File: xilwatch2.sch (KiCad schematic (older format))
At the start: 1 part

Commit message: More work, mostly copied from rev1
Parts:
- added BT?: Battery_Cell, symbol Device:Battery_Cell
- added C? (x5): 0.1uF, symbol Device:C_Small
- added D?: LED_TopLeft, symbol Device_Extra:LED_RGBA
- added D?: LED_TopRight, symbol Device_Extra:LED_RGBA
- added D?: LED_BottomLeft, symbol Device_Extra:LED_RGBA
- added D?: LED_BottomRight, symbol Device_Extra:LED_RGBA
- added J?: Conn_SWD, symbol Connector_Generic:Conn_01x04
- added M?: Vibrator, symbol Motor:Motor_DC
- added Q?: BSS138, Package_TO_SOT_SMD:SOT-23, symbol Transistor_FET:BSS138
- added R? (x2): 10K, symbol Device:R_Small
- added R? (x12): 360R, symbol Device:R_Small
- added SW?: Btn_Up, symbol Switch:SW_Push
- added SW?: Btn_Select, symbol Switch:SW_Push
- added SW?: Btn_Down, symbol Switch:SW_Push
- added SW?: Btn_Back, symbol Switch:SW_Push
- added U?: MPU-6500, symbol Sensor_Motion_Extra:MPU-6500
- added U?: LPH7366, symbol Display_Graphic_Extra:LPH7366
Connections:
- net labels added: +BATT, BTN_BACK, BTN_DOWN, BTN_SELECT, BTN_UP, LCD_CS, LCD_DC, LCD_DIN, LCD_RESET, LCD_SCK, LED1_B, LED1_G, LED1_R, LED2_B, LED2_G, LED2_R, LED3_B, LED3_G, LED3_R, LED4_B, LED4_G, LED4_R, MPU_INT, MPU_SCL, MPU_SDA, SWDCLK, SWDIO, VDD, VIBRATOR
- wire segments 50 -> 147
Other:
- note added: "TODO:\n- USB connector\n- power stuff\n- USB connector\n- debug connector\n- LEDs\n- connectivity?\n- speaker?"

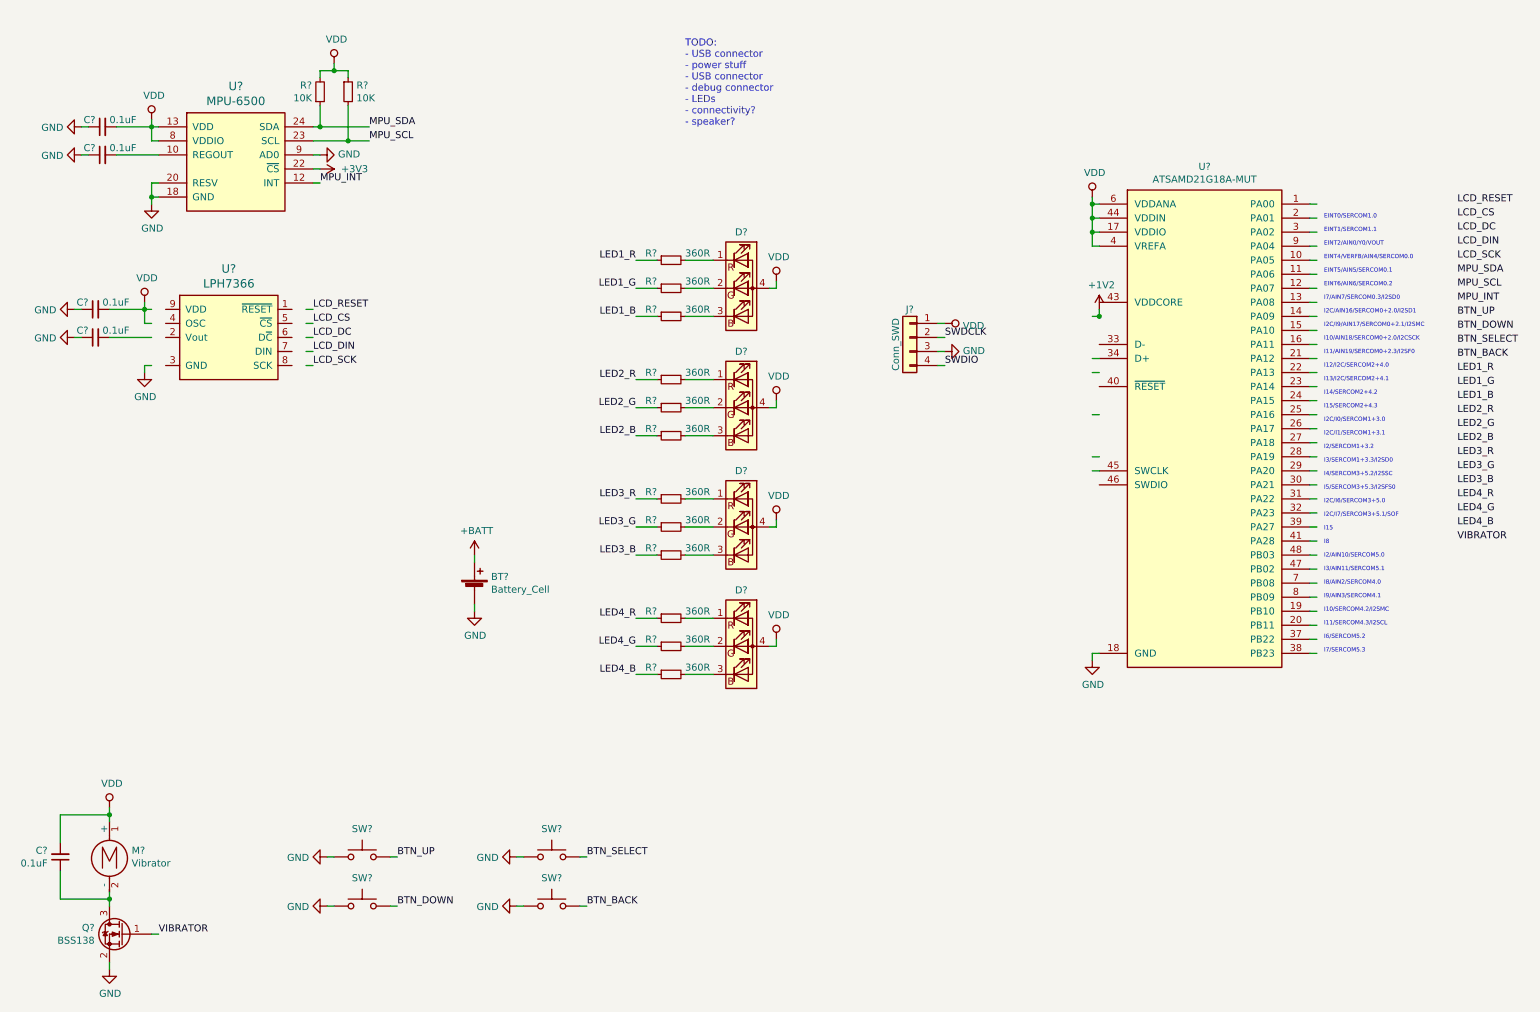
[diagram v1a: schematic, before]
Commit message: Finish power, usb, replace accel, add flash and assign footprints
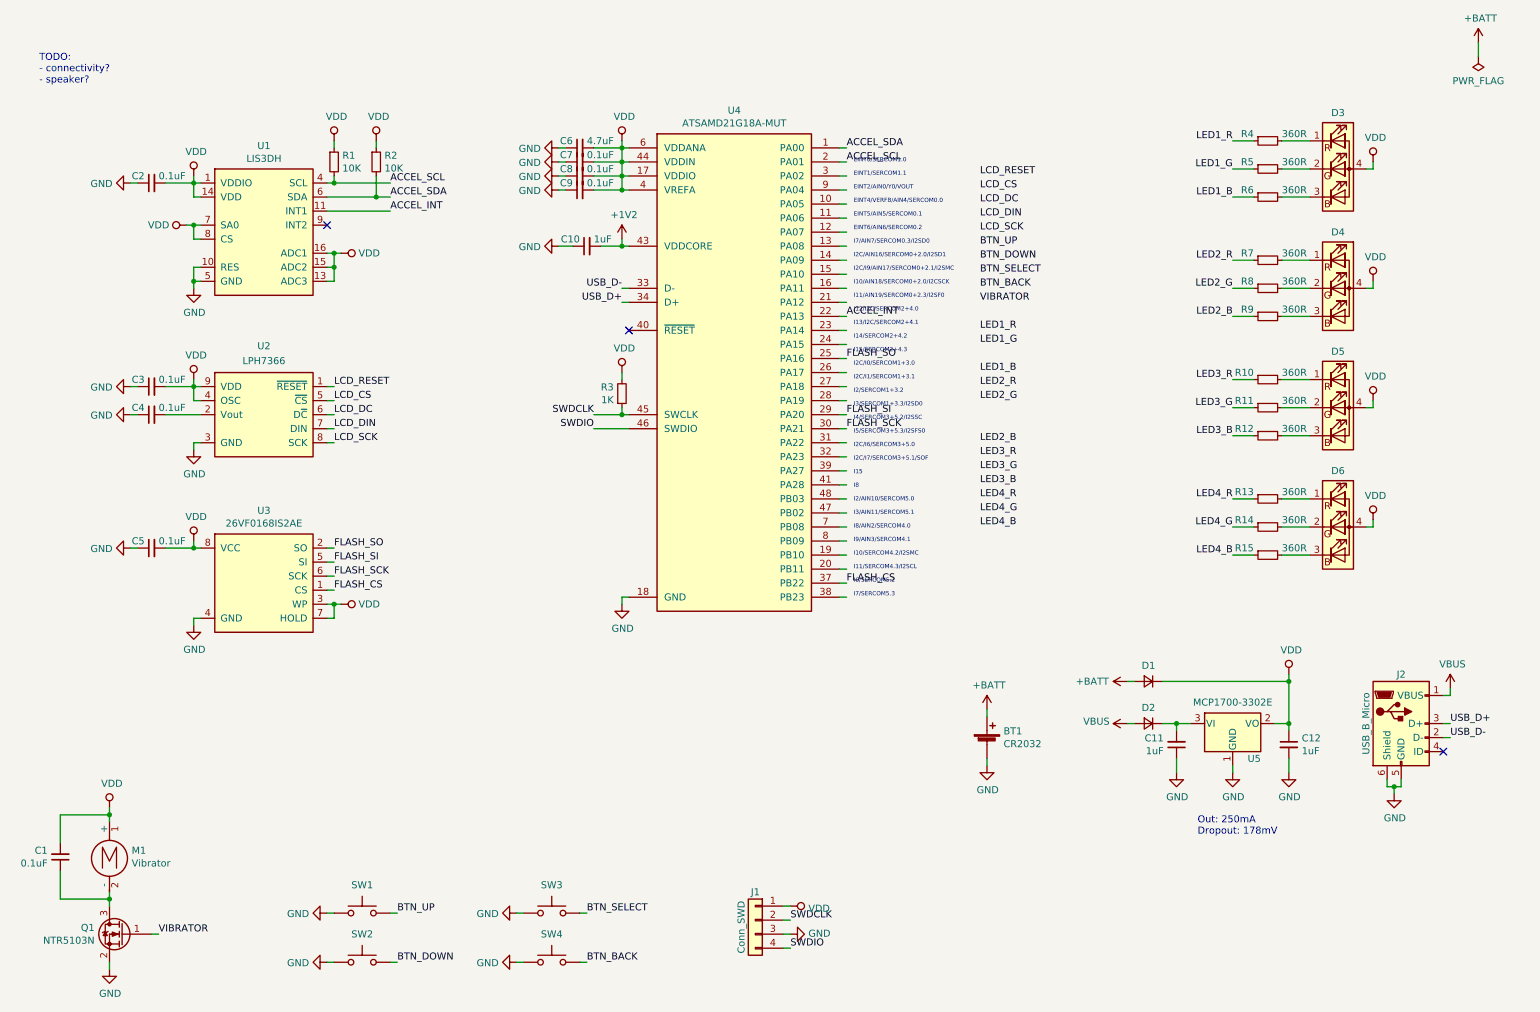
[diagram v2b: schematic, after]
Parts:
- removed C? (x2): 0.1uF, symbol Device:C_Small
- removed R? (x2): 10K, symbol Device:R_Small
- removed U?: MPU-6500, symbol Sensor_Motion_Extra:MPU-6500
- added C10, C11, C12: 1uF, Capacitor_SMD:C_0603_1608Metric, symbol Device:C_Small
- added C2, C5, C7, C8, C9: 0.1uF, Capacitor_SMD:C_0603_1608Metric, symbol Device:C_Small
- added C6: 4.7uF, Capacitor_SMD:C_0603_1608Metric, symbol Device:C_Small
- added D1, D2: S1JHE, Diode_SMD:D_SOD-323F, symbol Device:D_Small
- added J2: USB_B_Micro, Connector_USB:USB_Micro-B_Molex-105017-0001, symbol Connector:USB_B_Micro
- added R1, R2: 10K, Resistor_SMD:R_0603_1608Metric, symbol Device:R_Small
- added R3: 1K, Resistor_SMD:R_0603_1608Metric, symbol Device:R_Small
- added U1: LIS3DH, Package_LGA:LGA-16_3x3mm_P0.5mm_LayoutBorder3x5y, symbol Sensor_Motion_Extra:LIS3DH
- added U3: 26VF0168IS2AE, Package_SO:SOIJ-8_5.3x5.3mm_P1.27mm, symbol Memory_Flash_Extra:26VF0168IS2AE
- added U5: MCP1700-3302E, Package_TO_SOT_SMD:SOT-23, symbol Regulator_Linear:MCP1700-3302E_SOT23
- BT1: renamed from BT?; value Battery_Cell -> CR2032; footprint (none) -> Battery_Extra:BAT-HLD-001
- C1, C3, C4: renamed from C?; footprint (none) -> Capacitor_SMD:C_0603_1608Metric
- D3, D4, D5, D6: renamed from D?; footprint (none) -> LED_SMD_Extra:LED_RGBA_0606
- J1: renamed from J?; footprint (none) -> Connector_JST:JST_SH_SM04B-SRSS-TB_1x04-1MP_P1.00mm_Horizontal
- M1: renamed from M?; footprint (none) -> Buzzer_Beeper_Extra:C1026B
- Q1: renamed from Q?; value BSS138 -> NTR5103N
- R10, R11, R12, R13, R14, R15, R4, R5, R6, R7, R8, R9: renamed from R?; footprint (none) -> Resistor_SMD:R_0603_1608Metric
- SW1, SW2, SW3, SW4: renamed from SW?; footprint (none) -> Button_Switch_SMD_Extra:KLS7-TS2402
- U2: renamed from U?; footprint (none) -> Display_Extra:Nokia_5110-3310_LCD
- gave numbers to parts that had none: 1
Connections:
- net labels added: ACCEL_INT, ACCEL_SCL, ACCEL_SDA, FLASH_CS, FLASH_SCK, FLASH_SI, FLASH_SO, USB_D+, USB_D-, VBUS
- net labels removed: +3V3, MPU_INT, MPU_SCL, MPU_SDA
- wire segments 147 -> 199
- no-connect marks 0 -> 3
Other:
- note added: "Out: 250mA\nDropout: 178mV"
- note added: "TODO:\n- connectivity?\n- speaker?"
- note removed: "TODO:\n- USB connector\n- power stuff\n- USB connector\n- debug connector\n- LEDs\n- connectivity?\n- speaker?"
- moved on the sheet: BT1, C3, C4, D3, D4, D5, D6, J1, R10, R11, R12, R13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
